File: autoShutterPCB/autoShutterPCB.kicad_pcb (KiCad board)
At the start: 2 copper layers, 39 x 54.5 mm, 10 parts, among them U1 XIAO-RP2040-DIP

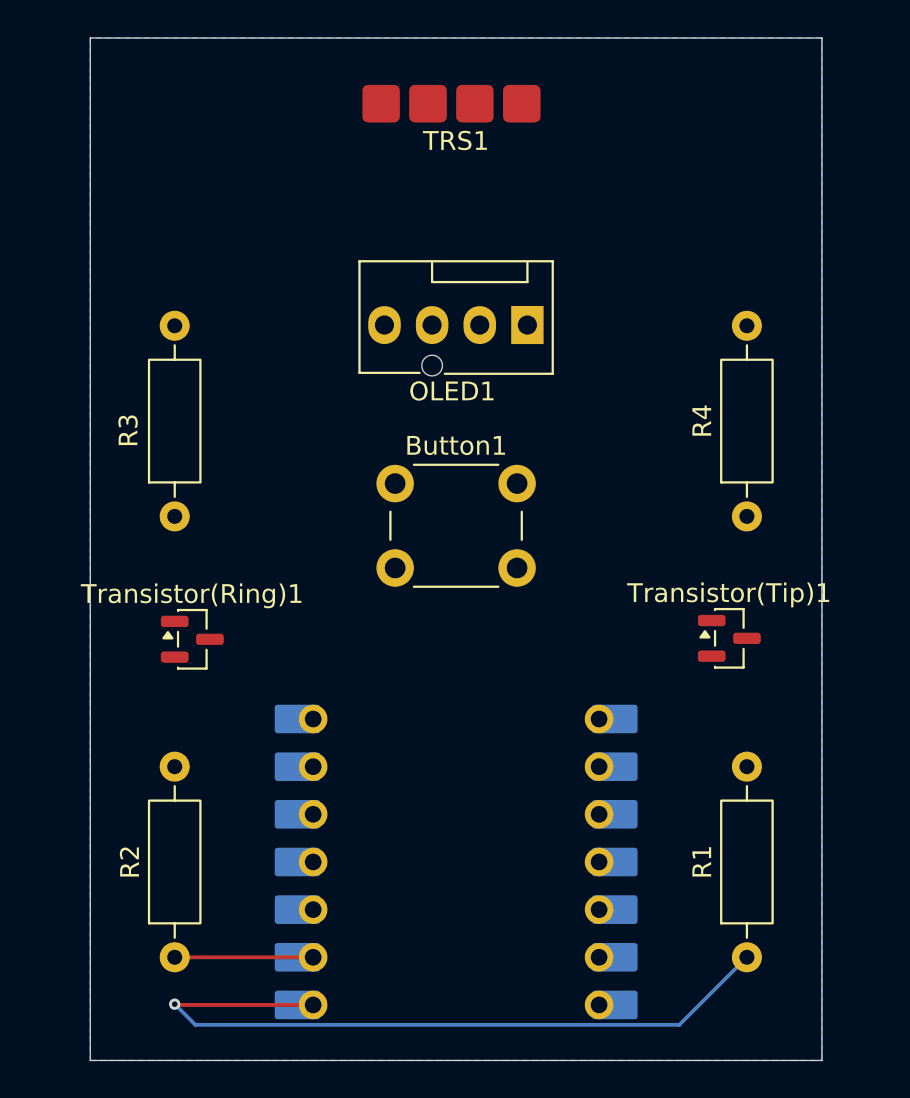
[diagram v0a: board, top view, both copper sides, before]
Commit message: Fix: Fix silkscreen for transistor
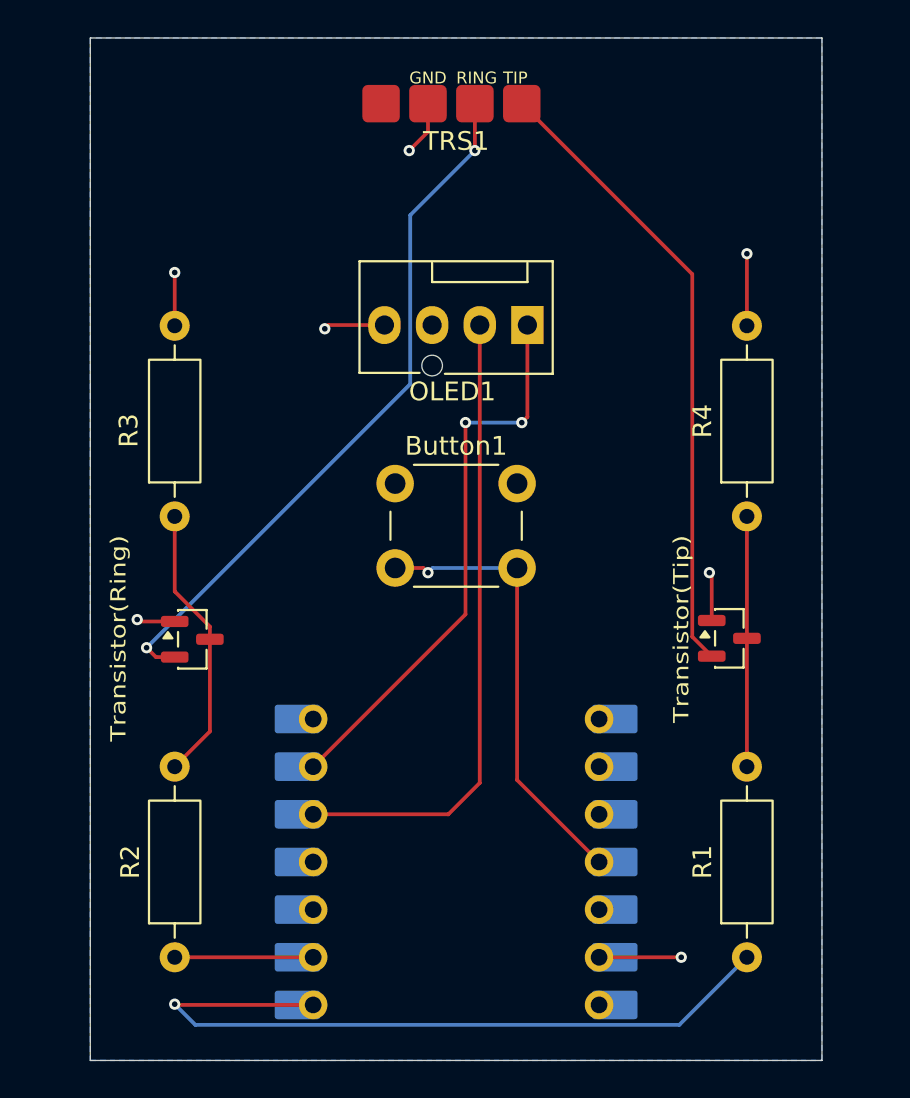
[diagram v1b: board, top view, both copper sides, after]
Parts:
- renumbered Transistor(Ring)1 to Transistor(Ring), Transistor(Tip)1 to Transistor(Tip)
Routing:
- net /ring: track 0.00 -> 38.0 mm, vias 0 -> 2
- net /sda: track 0.00 -> 34.0 mm
- net /tip: track 0.00 -> 33.6 mm
- net /scl: track 0.00 -> 30.0 mm, vias 0 -> 2
- net /d10B: track 0.00 -> 24.2 mm, vias 0 -> 1
- net GND: track 0.00 -> 21.9 mm, vias 0 -> 7
- net Net-(Transistor(Ring)1-B): track 0.00 -> 14.9 mm
- net Net-(Transistor(Tip)1-B): track 0.00 -> 13.3 mm
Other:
- board text added: "GND"
- board text added: "RING"
- board text added: "TIP"

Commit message: feat: Add mounting holes to design
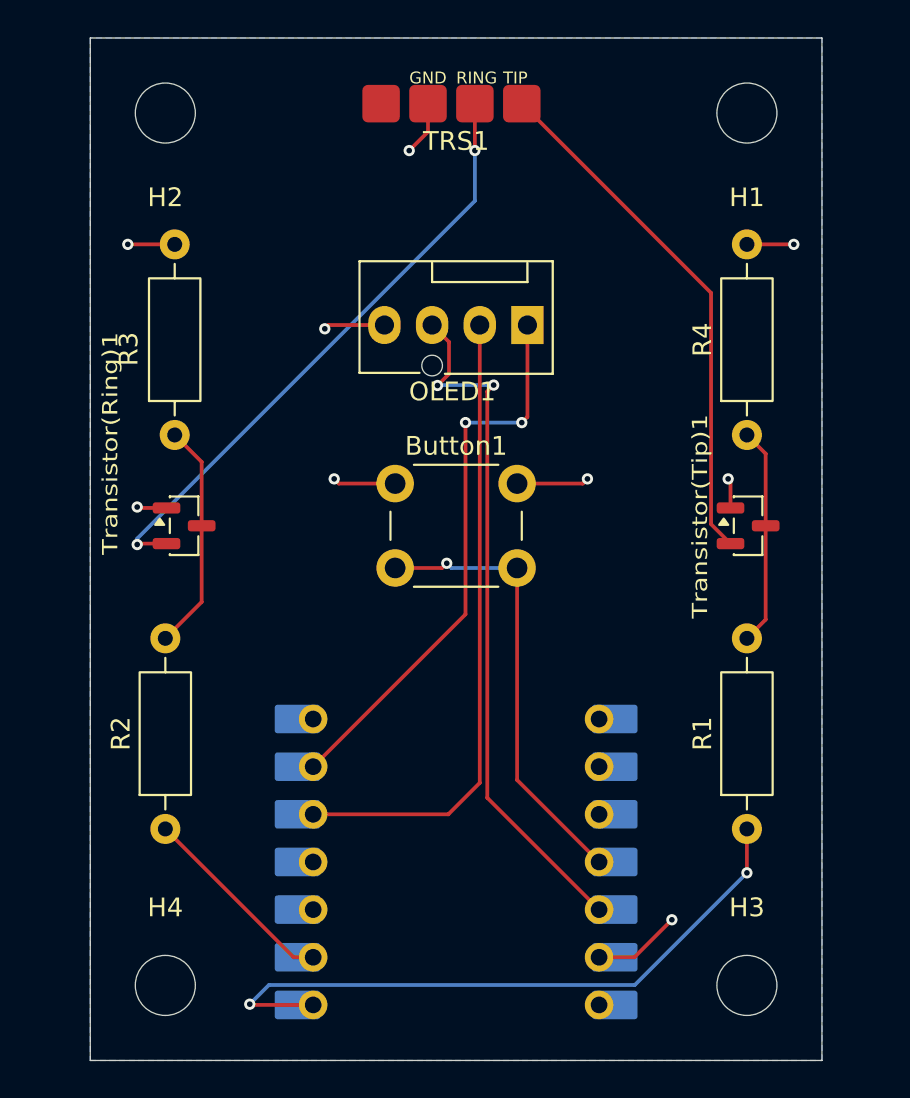
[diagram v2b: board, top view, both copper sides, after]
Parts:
- added H1: MountingHole, MountingHole:MountingHole_3.2mm_M3, F.Cu at (173.0, 75.0)
- added H2: MountingHole, MountingHole:MountingHole_3.2mm_M3, F.Cu at (142.0, 75.0)
- added H3: MountingHole, MountingHole:MountingHole_3.2mm_M3, F.Cu at (173.0, 121.5)
- added H4: MountingHole, MountingHole:MountingHole_3.2mm_M3, F.Cu at (142.0, 121.5)
- moved R2 6.86 mm to (142.0, 113.2)
- moved R1 6.84 mm to (173.0, 113.2)
- moved Transistor(Tip)1 6.08 mm to (173.1, 97.0)
- moved Transistor(Ring)1 6.07 mm to (143.0, 97.0)
- moved R3 4.34 mm to (142.5, 92.2)
- moved R4 4.34 mm to (173.0, 92.2)
- renumbered Transistor(Ring) to Transistor(Ring)1, Transistor(Tip) to Transistor(Tip)1
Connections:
- OLED1 pad 3: +3V3 -> /3.3
- U1 pad 12: unconnected-(U1-3V3-Pad12) -> /3.3
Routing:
- net /3.3: track 0.00 -> 37.4 mm, vias 0 -> 2
- net /tip: track 33.6 -> 28.1 mm
- net /ring: track 38.0 -> 32.5 mm
- net /d0: track 39.8 -> 35.1 mm, vias 1 -> 2
- net GND: track 21.9 -> 26.3 mm, vias 7 -> 9
- net /d1: track 7.38 -> 10.7 mm
- net Net-(Transistor(Ring)1-B): track 14.9 -> 12.2 mm
- net Net-(Transistor(Tip)1-B): track 13.3 -> 11.7 mm
